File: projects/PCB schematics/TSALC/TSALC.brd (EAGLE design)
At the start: 160 x 100 mm, 27 parts, among them IC2 78L08SMD, IC4 NE555D, Q1 IRLZ44Z, Q2 IRLZ44Z, Q3 IRLZ44Z

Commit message: FUSE - Board build update.
Fuse board design updated for 91 connector points.
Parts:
- moved GREEN1 166.5 mm to (109.2, 12.1)
- moved NOT 146.2 mm to (111.9, 49.5)
- moved OK1 141.0 mm to (83.8, 33.0)
- moved C1 129.9 mm to (100.3, 90.2)
- moved C4 129.9 mm to (85.1, 90.2)
- moved C6 129.9 mm to (69.8, 90.2)
- moved HV-OPA 116.1 mm to (97.8, 62.2)
- moved JP1 111.6 mm to (83.8, 50.8)
- moved RED 110.8 mm to (92.7, 12.1)
- moved C2 88.9 mm to (39.4, 50.8)
- moved C3 88.9 mm to (33.0, 50.8)
- moved C5 88.9 mm to (45.7, 50.8)
- moved C7 88.9 mm to (26.7, 50.8)
- moved C8 88.9 mm to (71.1, 59.7)
- moved R1 88.9 mm to (35.6, 57.1)
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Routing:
- net HV-: track 0.00 -> 287.2 mm, vias 0 -> 3
- net V+: track 0.00 -> 197.3 mm, vias 0 -> 4
- net +8V: track 0.00 -> 186.6 mm, vias 0 -> 2
- net GND: track 0.00 -> 181.7 mm, vias 0 -> 4
- net VTIMER: track 0.00 -> 157.7 mm
- net +60VDANGER-FLASHRED: track 0.00 -> 150.4 mm, vias 0 -> 1
- net N$8: track 0.00 -> 111.2 mm, vias 0 -> 1
- net +12V: track 0.00 -> 109.9 mm
- net THR: track 0.00 -> 104.3 mm, vias 0 -> 2
- net SAFESIGNAL-SOLIDGREEN: track 0.00 -> 96.2 mm, vias 0 -> 2
- net N$9: track 0.00 -> 89.8 mm
- net N$3: track 0.00 -> 77.6 mm
- net N$5: track 0.00 -> 74.0 mm
- net N$4: track 0.00 -> 69.7 mm
- net N$6: track 0.00 -> 51.6 mm
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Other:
- board text added: "Tractive System Active Light(TSAL) Circuit Board: Rev A. Date: 28th March 2019"

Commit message: TSALC - Initial build.
Initial build done by Anshuman. 
TSALC is still WIP.
TSALC work must be continued on another branch.
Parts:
- R1: value (none) -> 10k
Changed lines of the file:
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@@
 <attribute name="VALUE" x="12.573" y="16.51" size="1.778" layer="27" ratio="10"/>
 </element>
-<element name="R1" library="rcl" library_urn="urn:adsk.eagle:library:334" package="R0805" package3d_urn="urn:adsk.eagle:package:23553/2" value="" x="35.56" y="57.15" smashed="yes">
+<element name="R1" library="rcl" library_urn="urn:adsk.eagle:library:334" package="R0805" package3d_urn="urn:adsk.eagle:package:23553/2" value="10k" x="35.56" y="57.15" smashed="yes">
 <attribute name="NAME" x="34.925" y="58.42" size="1.27" layer="25"/>
 <attribute name="SPICEPREFIX" value="R" x="88.9" y="1.27" size="1.778" layer="27" display="off"/>

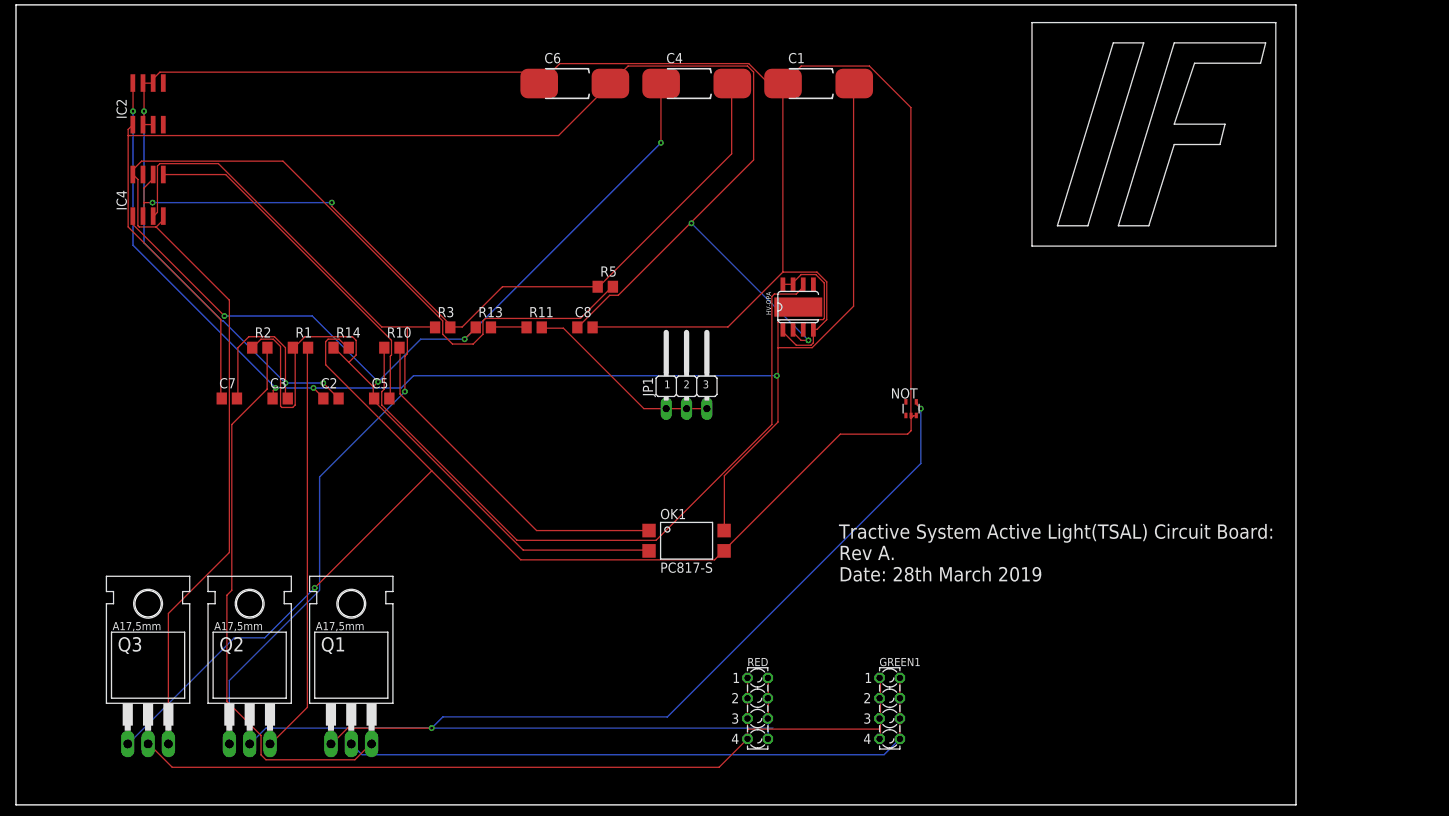
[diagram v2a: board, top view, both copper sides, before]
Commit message: Minor board update
Cleared up come wiring conflicts
Board Schematic Update

555 Timer Circuit changed accordingly.
(ref. https://www.allaboutcircuits.com/tools/555-timer-astable-circuit/)
Flash Frequency = 4.80 Hz
Duty Cycle = 66.67%
Board Revision Update( Rev B)

Both board and schematic updated.
Clearance issues still remain.
Some component values need to be verified again.
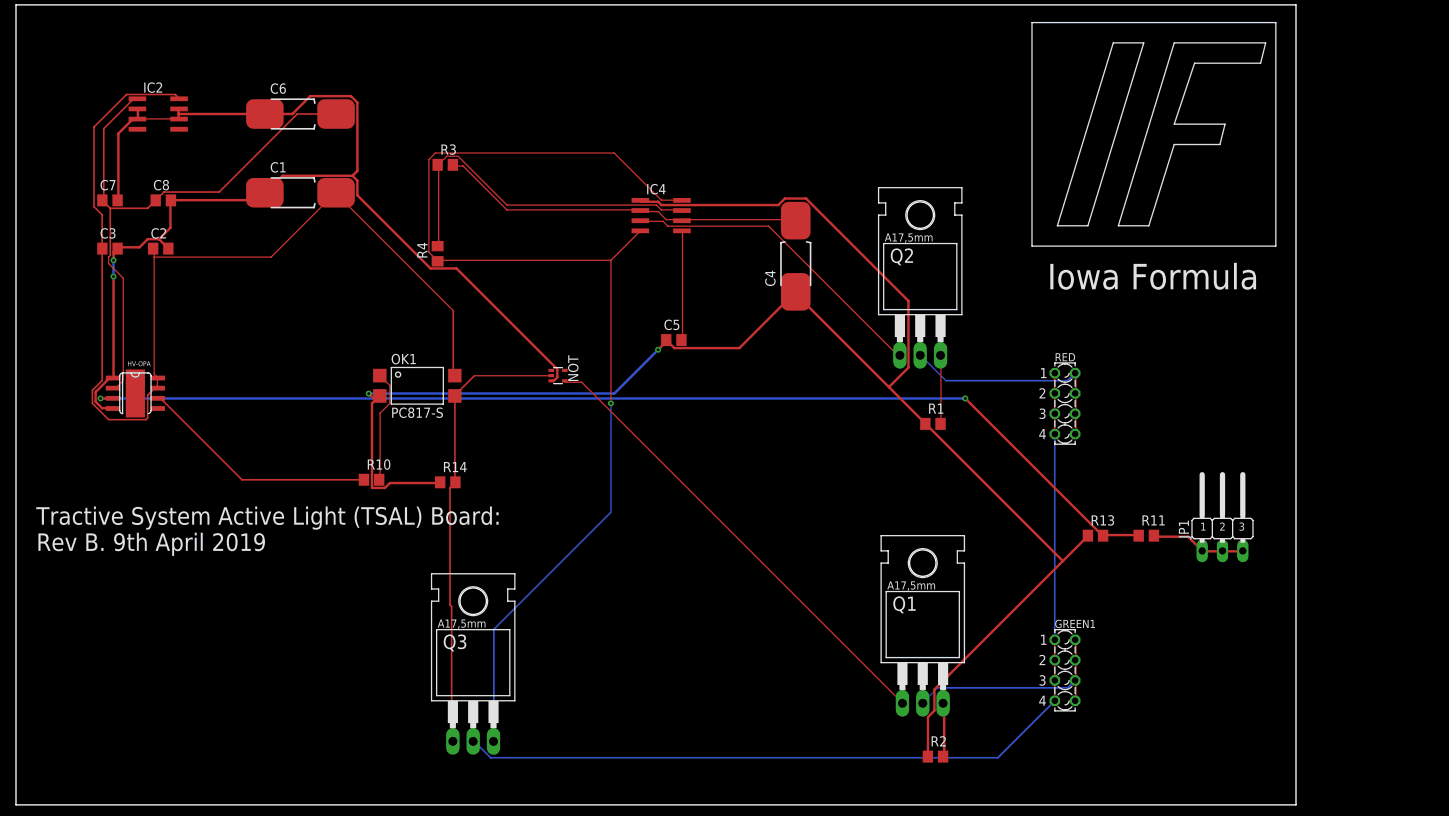
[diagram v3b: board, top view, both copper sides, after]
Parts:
- removed R5: (no value), rcl:R0805
- added R4: 50k, rcl:R0805
- C4: value 10uF -> 2uF
- R2: value (none) -> 10k
- R3: value 15k -> 50k
- moved R2 98.7 mm to (114.9, 6.03)
- moved Q2 96.9 mm to (113.0, 62.5)
- moved HV-OPA 83.6 mm to (14.9, 51.4), turned to 270 degrees
- moved R11 80.8 mm to (141.3, 33.7)
- moved R13 80.8 mm to (134.9, 33.7)
- moved R1 79.6 mm to (114.6, 47.6)
- moved Q1 71.6 mm to (113.3, 19.1)
- moved JP1 69.3 mm to (150.8, 33.0)
- moved C1 66.2 mm to (35.6, 76.5)
- moved IC4 64.2 mm to (80.6, 73.7), turned to 270 degrees
- moved C8 55.0 mm to (18.4, 75.6)
- moved RED 54.1 mm to (131.1, 50.2)
- moved NOT 44.3 mm to (67.8, 53.7), turned to 270 degrees
- moved Q3 40.6 mm to (57.1, 14.3)
- moved OK1 38.8 mm to (50.2, 52.4)
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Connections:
- removed net VDIV_SIGNAL: R11.1, R13.2
- new net N$2: IC4.7, R3.1, R4.2
- net N$8: no longer R3.1
- net SIGNAL_VDIV: now also R11.1, R13.2
- net THR: no longer R5.1
- net VTIMER: now also R4.1; no longer R5.2
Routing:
- net SIGNAL_VDIV: track 0.00 -> 138.5 mm, vias 0 -> 2
- net HV-: track 287.2 -> 150.9 mm, vias 3 -> 2
- net +8V: track 186.6 -> 73.5 mm, vias 2 -> 0
- net +60VDANGER-FLASHRED: track 150.4 -> 56.7 mm, vias 1 -> 0
- net N$8: track 111.2 -> 39.5 mm, vias 1 -> 0
- net V+: track 197.3 -> 133.2 mm, vias 4 -> 0
- net N$4: track 69.7 -> 6.83 mm
- net N$9: track 89.8 -> 30.2 mm
- net THR: track 104.3 -> 45.9 mm, vias 2 -> 0
- net N$3: track 77.6 -> 28.1 mm
- net N$5: track 74.0 -> 28.9 mm
- net N$2: track 0.00 -> 44.1 mm
- net N$6: track 51.6 -> 8.59 mm
- net SAFESIGNAL-SOLIDGREEN: track 96.2 -> 59.0 mm, vias 2 -> 0
- net GND: track 181.7 -> 216.7 mm, vias 4 -> 2
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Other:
- board text added: "Iowa Formula"
- board text added: "Tractive System Active Light (TSAL) Board: Rev B. 9th April 2019"
- board text removed: "Tractive System Active Light(TSAL) Circuit Board: Rev A. Date: 28th March 2019"
